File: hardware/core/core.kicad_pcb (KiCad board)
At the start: 2 copper layers, 228.6 x 129.5 mm, 102 parts, among them J1 9V_IN, J2 MIDI IN, J3 MIDI OUT 1, J4 SWITCHES OUT, J5 EXP/AUX IN, J7 LCD, J8 USB_C_Receptacle_USB2.0_16P, J9 MIDI OUT 2/3, K1 G5V-1, K2 G5V-1, Q3 2N3904, Q4 2N3904, SW1 FS, SW10 BOOT, SW2 FS, SW3 FS, SW4 FS, SW5 FS, SW6 FS, SW7 FS, SW8 FS, SW9 RESET, U1 LM2596S-5, U2 6N137, U3 ESP32-S3-WROOM-1, U4 LD1117-3.3V-SOT223, U5 USBLC6-2SC6, U6 74HCT04

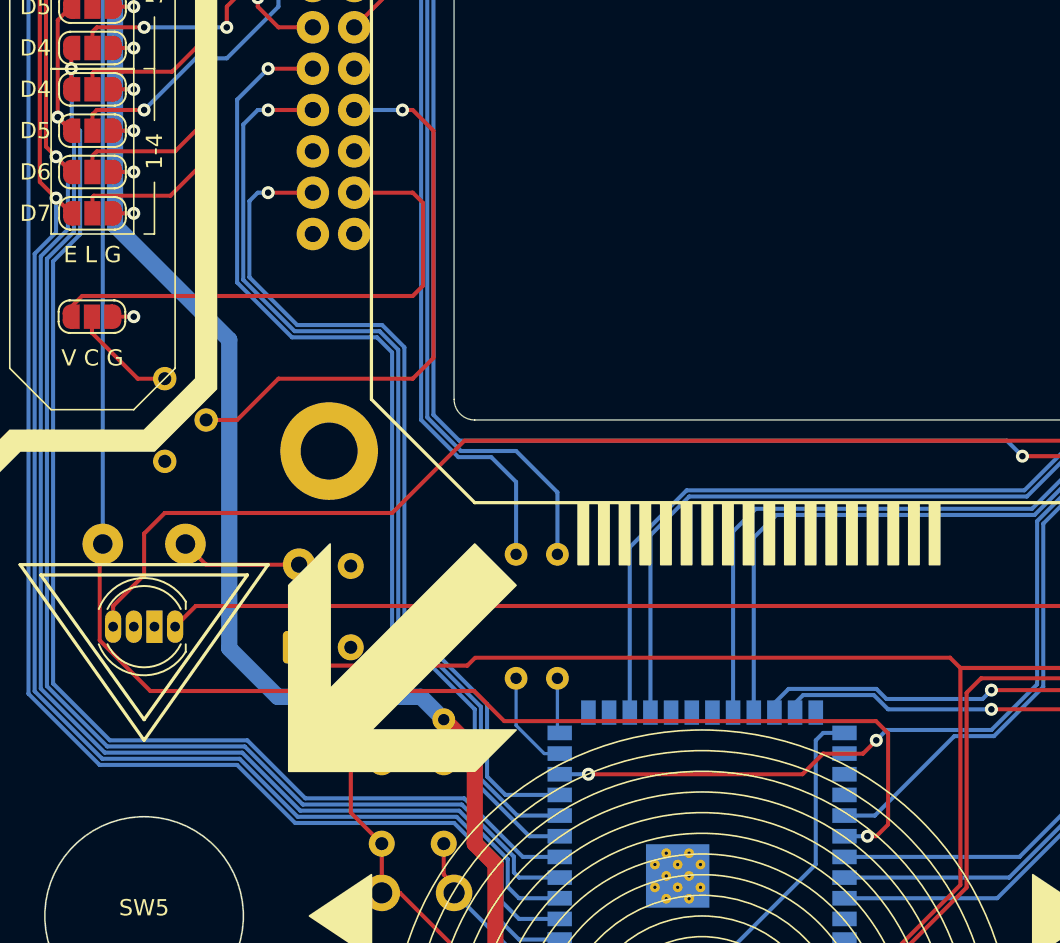
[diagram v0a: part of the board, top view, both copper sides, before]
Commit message: Add switch matrix GPIO configuration and hardware updates
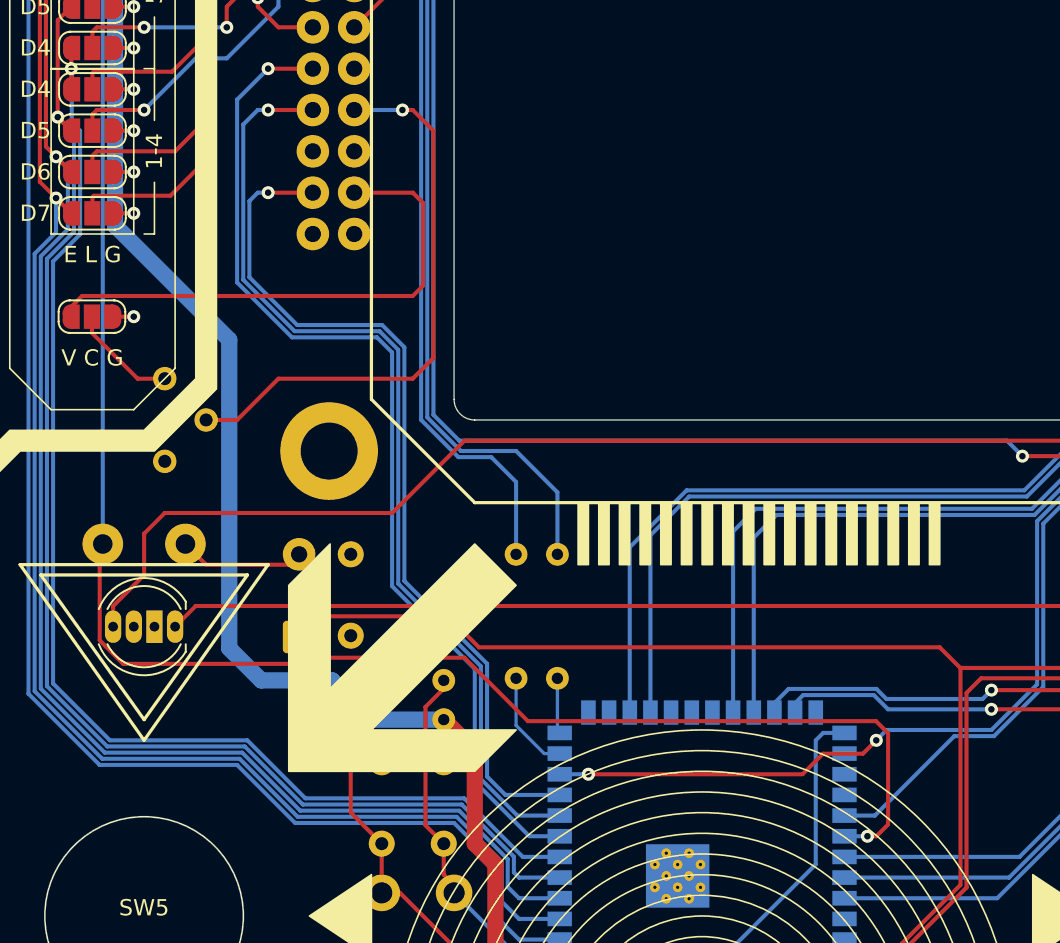
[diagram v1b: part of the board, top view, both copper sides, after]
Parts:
- added R17: 10K, Resistor_THT:R_Axial_DIN0204_L3.6mm_D1.6mm_P7.62mm_Horizontal, B.Cu at (111.1, 190.0)
- moved C12 0.72 mm to (113.0, 182.2)
- moved D15 0.64 mm to (109.9, 187.3)
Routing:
- net RESET: track 12.4 -> 23.4 mm
- net R2: track 239.8 -> 241.6 mm
